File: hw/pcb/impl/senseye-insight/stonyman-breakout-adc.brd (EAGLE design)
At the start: 30.5 x 9.8 mm, 8 parts

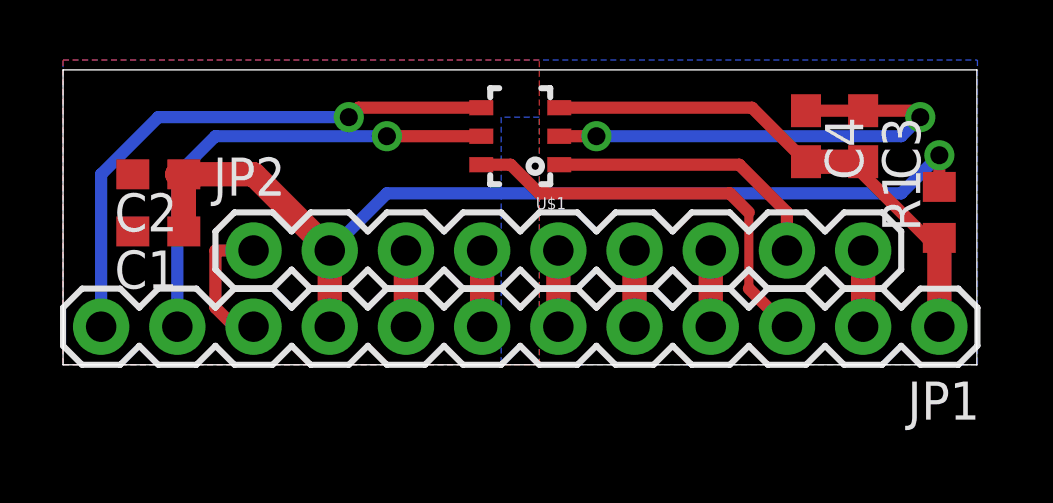
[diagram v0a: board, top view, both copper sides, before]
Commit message: better isolation of the SPI lines and GND
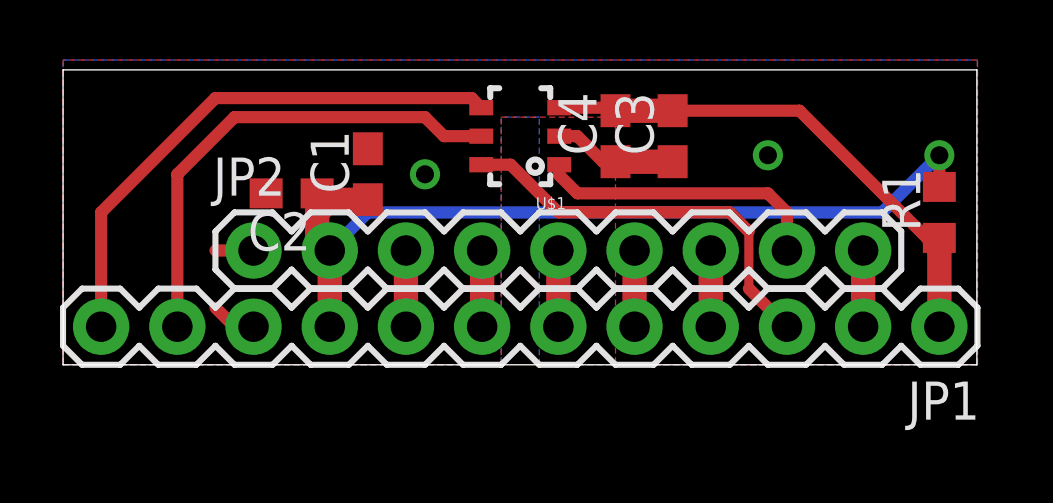
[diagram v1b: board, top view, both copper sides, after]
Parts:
- moved C1 7.24 mm to (10.2, 6.35), turned to 90 degrees
- moved C3 6.35 mm to (20.3, 7.62), turned to 90 degrees
- moved C4 6.35 mm to (18.4, 7.62), turned to 90 degrees
- moved C2 4.49 mm to (7.62, 5.71)
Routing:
- net GND: track 20.9 -> 6.97 mm
- net V_STONY: track 35.3 -> 29.2 mm
- net V_ADC: track 17.3 -> 18.0 mm
- net ADC-MISO: track 15.7 -> 16.3 mm, vias 1 -> 0
- net ADC-SCLK: track 18.7 -> 18.2 mm, vias 1 -> 0

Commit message: pretty sure this is finished but needs to pass DRC
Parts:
- moved C1 0.63 mm to (10.2, 5.71), turned to 0 degrees
- moved C2 0.63 mm to (6.99, 5.71)
- moved C3 0.63 mm to (20.3, 6.99)
- moved C4 0.63 mm to (18.4, 6.99)
- moved U$1 0.63 mm to (15.2, 6.99)
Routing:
- net V_STONY: track 29.2 -> 30.6 mm
- net ADC-MISO: track 16.3 -> 17.6 mm
- net ANALOG: track 9.72 -> 8.88 mm
- net GND: track 6.97 -> 6.94 mm, vias 2 -> 3

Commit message: added one more extra piece of GND routing
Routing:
- net GND: track 6.94 -> 9.48 mm
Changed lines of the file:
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@@
 <via x="12.7" y="5.715" extent="1-16" drill="0.6"/>
 <via x="3.81" y="4.445" extent="1-16" drill="0.6"/>
+<wire x1="6.35" y1="3.81" x2="6.35" y2="6.35" width="0.4064" layer="1"/>
 </signal>
 <signal name="V_STONY">

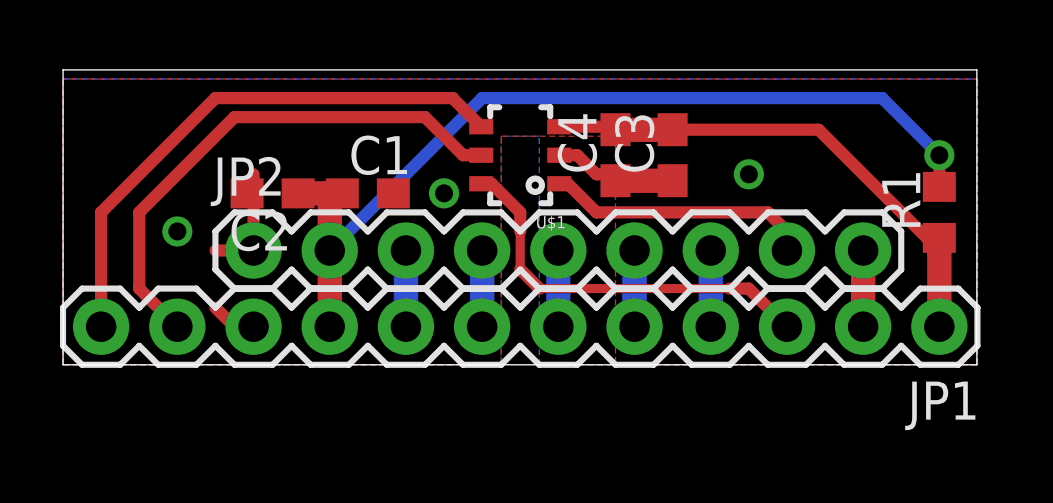
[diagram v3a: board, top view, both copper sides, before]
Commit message: made the board even tighter
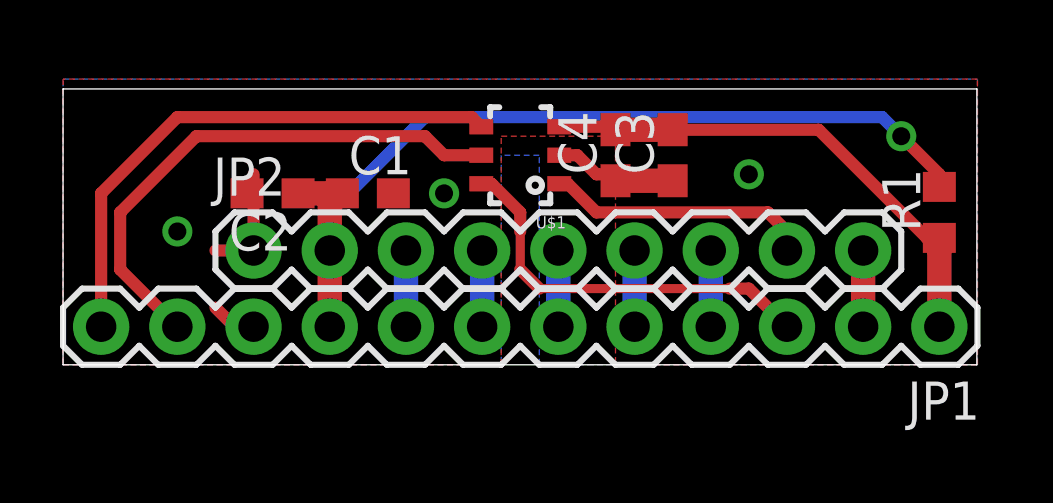
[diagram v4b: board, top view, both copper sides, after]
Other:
- board size 30.5 x 9.8 mm -> 30.5 x 9.2 mm
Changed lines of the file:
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@@
 <plain>
 <wire x1="0" y1="0" x2="30.46" y2="0" width="0" layer="20"/>
-<wire x1="30.46" y1="0" x2="30.46" y2="9.83" width="0" layer="20"/>
-<wire x1="30.46" y1="9.83" x2="0" y2="9.83" width="0" layer="20"/>
-<wire x1="0" y1="9.83" x2="0" y2="0" width="0" layer="20"/>
+<wire x1="30.46" y1="0" x2="30.46" y2="9.195" width="0" layer="20"/>
+<wire x1="30.46" y1="9.195" x2="0" y2="9.195" width="0" layer="20"/>
+<wire x1="0" y1="9.195" x2="0" y2="0" width="0" layer="20"/>
 </plain>
 <attributes>
@@
 </class>
 </classes>
-<designrules name="default">
-<description language="de">&lt;b&gt;EAGLE Design Rules&lt;/b&gt;
+<designrules name="sunstone-2lyr_v1.0.0.3">
+<description language="en">&lt;b&gt;EAGLE Design Rules for *2* Layer Designs (DS)&lt;/b&gt;
 &lt;p&gt;
-Die Standard-Design-Rules sind so gewählt, dass sie für
-die meisten Anwendungen passen. Sollte ihre Platine
-besondere Anforderungen haben, treffen Sie die erforderlichen
-Einstellungen hier und speichern die Design Rules unter
-einem neuen Namen ab.</description>
-<description language="en">&lt;b&gt;EAGLE Design Rules&lt;/b&gt;
+This Sunstone Circuits 2 Layer .DRU has been set to cover our minimum requirements for our double sided products. For questions, comments, suggestions, please contact Sunstone Customer Support: &lt;p&gt;&lt;b&gt;Email:&lt;/b&gt;  mailto:support@sunstone.com&lt;br&gt;&lt;b&gt;Phone:&lt;/b&gt; 800-228-8198.&lt;p&gt; v1.1Mod10/16/07~Layers-core reversal.Distance C/D.Restring%.Supply G%.&lt;p&gt; v1.2 Mod12/06/07~Distance C/D to 20mils.&lt;p&gt;v1.3Mod12/12/07~Supply/Annulus Value to 12.5mils&lt;p&gt;1/15/08 SSC-EAGLE-2Lyr_v1.0.0.3~For Release&lt;p&gt;10/3/08 Description Edit.&lt;p&gt;
 &lt;p&gt;
-The default Design Rules have been set to cover
-a wide range of applications. Your particular design
-may have different requirements, so please make the
-necessary adjustments and save your customized
-design rules under a new name.</description>
+&lt;i&gt;Attention: Upon running the design check and making modifications, please remember to save any changes before closing the application and sending in your board file to Sunstone Circuits for conversion.&lt;i&gt;</description>
 <param name="layerSetup" value="(1*16)"/>
-<param name="mtCopper" value="0.035mm 0.035mm 0.035mm 0.035mm 0.035mm 0.035mm 0.035mm 0.035mm 0.035mm 0.035mm 0.035mm 0.035mm 0.035mm 0.035mm 0.035mm 0.035mm"/>
-<param name="mtIsolate" value="1.5mm 0.15mm 0.2mm 0.15mm 0.2mm 0.15mm 0.2mm 0.15mm 0.2mm 0.15mm 0.2mm 0.15mm 0.2mm 0.15mm 0.2mm"/>
-<param name="mdWireWire" value="8mil"/>
-<param name="mdWirePad" value="8mil"/>
-<param name="mdWireVia" value="8mil"/>
-<param name="mdPadPad" value="8mil"/>
-<param name="mdPadVia" value="8mil"/>
-<param name="mdViaVia" value="8mil"/>
-<param name="mdSmdPad" value="8mil"/>
-<param name="mdSmdVia" value="8mil"/>
-<param name="mdSmdSmd" value="8mil"/>
+<param name="mtCopper" value="0.0178mm 0.0356mm 0.0356mm 0.0356mm 0.0356mm 0.0356mm 0.0356mm 0.0356mm 0.0356mm 0.0356mm 0.0356mm 0.0356mm 0.0356mm 0.0356mm 0.0356mm 0.0178mm"/>
+<param name="mtIsolate" value="59mil 0.1499mm 0.2007mm 0.1499mm 0.2007mm 0.1499mm 0.2007mm 0.1499mm 0.2007mm 0.1499mm 0.2007mm 0.1499mm 0.2007mm 0.1499mm 0.2007mm"/>
+<param name="mdWireWire" value="6mil"/>
+<param name="mdWirePad" value="6mil"/>
+<param name="mdWireVia" value="6mil"/>
+<param name="mdPadPad" value="6mil"/>
+<param name="mdPadVia" value="6mil"/>
+<param name="mdViaVia" value="6mil"/>
+<param name="mdSmdPad" value="6mil"/>
+<param name="mdSmdVia" value="6mil"/>
+<param name="mdSmdSmd" value="6mil"/>
 <param name="mdViaViaSameLayer" value="8mil"/>
 <param name="mnLayersViaInSmd" value="2"/>
-<param name="mdCopperDimension" value="40mil"/>
-<param name="mdDrill" value="8mil"/>
+<param name="mdCopperDimension" value="20mil"/>
+<param name="mdDrill" value="16mil"/>
 <param name="mdSmdStop" value="0mil"/>
-<param name="msWidth" value="10mil"/>
-<param name="msDrill" value="24mil"/>
-<param name="msMicroVia" value="9.99mm"/>
+<param name="msWidth" value="6mil"/>
+<param name="msDrill" value="14mil"/>
+<param name="msMicroVia" value="9.9898mm"/>
 <param name="msBlindViaRatio" value="0.5"/>
 <param name="rvPadTop" value="0.25"/>
@@
 <param name="rvMicroViaOuter" value="0.25"/>
 <param name="rvMicroViaInner" value="0.25"/>
-<param name="rlMinPadTop" value="10mil"/>
-<param name="rlMaxPadTop" value="20mil"/>
-<param name="rlMinPadInner" value="10mil"/>
-<param name="rlMaxPadInner" value="20mil"/>
-<param name="rlMinPadBottom" value="10mil"/>
-<param name="rlMaxPadBottom" value="20mil"/>
+<param name="rlMinPadTop" value="8mil"/>
+<param name="rlMaxPadTop" value="999mil"/>
+<param name="rlMinPadInner" value="0mil"/>
+<param name="rlMaxPadInner" value="0mil"/>
+<param name="rlMinPadBottom" value="8mil"/>
+<param name="rlMaxPadBottom" value="999mil"/>
 <param name="rlMinViaOuter" value="8mil"/>
-<param name="rlMaxViaOuter" value="20mil"/>
-<param name="rlMinViaInner" value="8mil"/>
-<param name="rlMaxViaInner" value="20mil"/>
-<param name="rlMinMicroViaOuter" value="4mil"/>
-<param name="rlMaxMicroViaOuter" value="20mil"/>
-<param name="rlMinMicroViaInner" value="4mil"/>
-<param name="rlMaxMicroViaInner" value="20mil"/>
+<param name="rlMaxViaOuter" value="999mil"/>
+<param name="rlMinViaInner" value="0mil"/>
+<param name="rlMaxViaInner" value="0mil"/>
+<param name="rlMinMicroViaOuter" value="8mil"/>
+<param name="rlMaxMicroViaOuter" value="999mil"/>
+<param name="rlMinMicroViaInner" value="0mil"/>
+<param name="rlMaxMicroViaInner" value="0mil"/>
 <param name="psTop" value="-1"/>
 <param name="psBottom" value="-1"/>
@@
 <param name="mvStopFrame" value="1"/>
 <param name="mvCreamFrame" value="0"/>
-<param name="mlMinStopFrame" value="4mil"/>
-<param name="mlMaxStopFrame" value="4mil"/>
+<param name="mlMinStopFrame" value="3mil"/>
+<param name="mlMaxStopFrame" value="3mil"/>
 <param name="mlMinCreamFrame" value="0mil"/>
 <param name="mlMaxCreamFrame" value="0mil"/>
@@
 <param name="checkRestrict" value="1"/>
 <param name="useDiameter" value="13"/>
-<param name="maxErrors" value="50"/>
+<param name="maxErrors" value="500"/>
 </designrules>
 <autorouter>
@@
 <vertex x="30.48" y="0"/>
 <vertex x="15.875" y="0"/>
-<vertex x="15.875" y="7.62"/>
-<vertex x="14.605" y="7.62"/>
+<vertex x="15.875" y="6.985"/>
+<vertex x="14.605" y="6.985"/>
 <vertex x="14.605" y="0"/>
 <vertex x="0" y="0"/>
@@
 <contactref element="JP2" pad="2"/>
 <wire x1="8.89" y1="1.27" x2="8.89" y2="3.81" width="0.8128" layer="1"/>
-<via x="29.21" y="6.985" extent="1-16" drill="0.6"/>
-<wire x1="29.21" y1="6.985" x2="29.21" y2="5.93" width="0.4064" layer="1"/>
-<wire x1="8.89" y1="3.81" x2="13.97" y2="8.89" width="0.4064" layer="16"/>
-<wire x1="13.97" y1="8.89" x2="27.305" y2="8.89" width="0.4064" layer="16"/>
-<wire x1="27.305" y1="8.89" x2="29.21" y2="6.985" width="0.4064" layer="16"/>
 <wire x1="7.835" y1="5.715" x2="9.31" y2="5.715" width="0.8128" layer="1"/>
 <wire x1="9.31" y1="5.715" x2="8.89" y2="5.715" width="0.8128" layer="1"/>
 <wire x1="8.89" y1="5.715" x2="8.89" y2="3.81" width="0.8128" layer="1"/>
+<wire x1="29.21" y1="5.93" x2="29.21" y2="6.35" width="0.4064" layer="1"/>
+<wire x1="29.21" y1="6.35" x2="27.94" y2="7.62" width="0.4064" layer="1"/>
+<via x="27.94" y="7.62" extent="1-16" drill="0.6"/>
+<wire x1="27.94" y1="7.62" x2="27.305" y2="8.255" width="0.4064" layer="16"/>
+<wire x1="27.305" y1="8.255" x2="12.065" y2="8.255" width="0.4064" layer="16"/>
+<wire x1="12.065" y1="8.255" x2="8.89" y2="5.08" width="0.4064" layer="16"/>
+<wire x1="8.89" y1="5.08" x2="8.89" y2="3.81" width="0.4064" layer="16"/>
 </signal>
 <signal name="RESP">
@@
 <contactref element="U$1" pad="5"/>
 <contactref element="JP1" pad="11"/>
-<wire x1="13.94" y1="6.985" x2="13.335" y2="6.985" width="0.4064" layer="1"/>
-<wire x1="13.335" y1="6.985" x2="12.065" y2="8.255" width="0.4064" layer="1"/>
-<wire x1="12.065" y1="8.255" x2="5.715" y2="8.255" width="0.4064" layer="1"/>
-<wire x1="5.715" y1="8.255" x2="2.54" y2="5.08" width="0.4064" layer="1"/>
-<wire x1="2.54" y1="5.08" x2="2.54" y2="2.54" width="0.4064" layer="1"/>
-<wire x1="2.54" y1="2.54" x2="3.81" y2="1.27" width="0.4064" layer="1"/>
+<wire x1="13.94" y1="6.985" x2="12.7" y2="6.985" width="0.4064" layer="1"/>
+<wire x1="12.7" y1="6.985" x2="12.065" y2="7.62" width="0.4064" layer="1"/>
+<wire x1="12.065" y1="7.62" x2="4.445" y2="7.62" width="0.4064" layer="1"/>
+<wire x1="4.445" y1="7.62" x2="1.905" y2="5.08" width="0.4064" layer="1"/>
+<wire x1="1.905" y1="5.08" x2="1.905" y2="3.175" width="0.4064" layer="1"/>
+<wire x1="1.905" y1="3.175" x2="3.81" y2="1.27" width="0.4064" layer="1"/>
 </signal>
 <signal name="ADC-SCLK">
 <contactref element="U$1" pad="4"/>
 <contactref element="JP1" pad="12"/>
-<wire x1="13.94" y1="7.935" x2="12.985" y2="8.89" width="0.4064" layer="1"/>
-<wire x1="12.985" y1="8.89" x2="5.08" y2="8.89" width="0.4064" layer="1"/>
-<wire x1="5.08" y1="8.89" x2="1.27" y2="5.08" width="0.4064" layer="1"/>
-<wire x1="1.27" y1="5.08" x2="1.27" y2="1.27" width="0.4064" layer="1"/>
+<wire x1="13.94" y1="7.935" x2="13.62" y2="8.255" width="0.4064" layer="1"/>
+<wire x1="13.62" y1="8.255" x2="3.81" y2="8.255" width="0.4064" layer="1"/>
+<wire x1="3.81" y1="8.255" x2="1.27" y2="5.715" width="0.4064" layer="1"/>
+<wire x1="1.27" y1="5.715" x2="1.27" y2="1.27" width="0.4064" layer="1"/>
 </signal>
 <signal name="ADC-SS">

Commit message: fixed almost all the DRC errors
most were related to components and traces being too close to the board
edge. there are still some keepout errors (with 0603 caps which I won't
fix), and the analog line is justg a little too close to the headers
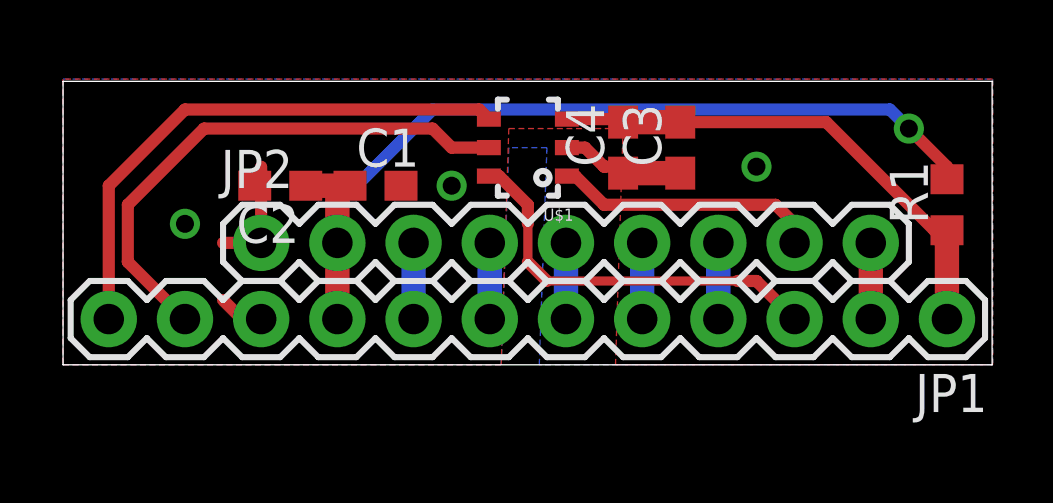
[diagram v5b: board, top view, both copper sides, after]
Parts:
- moved C3 0.36 mm to (20.6, 7.24)
- moved C4 0.36 mm to (18.7, 7.24)
- moved JP2 0.36 mm to (6.60, 4.06)
- moved C1 0.36 mm to (10.4, 5.97)
- moved C2 0.36 mm to (7.24, 5.97)
- moved U$1 0.36 mm to (15.5, 7.24)
- moved JP1 0.36 mm to (29.5, 1.52)
- moved R1 0.36 mm to (29.5, 5.33)
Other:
- board size 30.5 x 9.2 mm -> 31 x 9.4 mm

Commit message: fixed all DRC errors (including the 0603 caps)
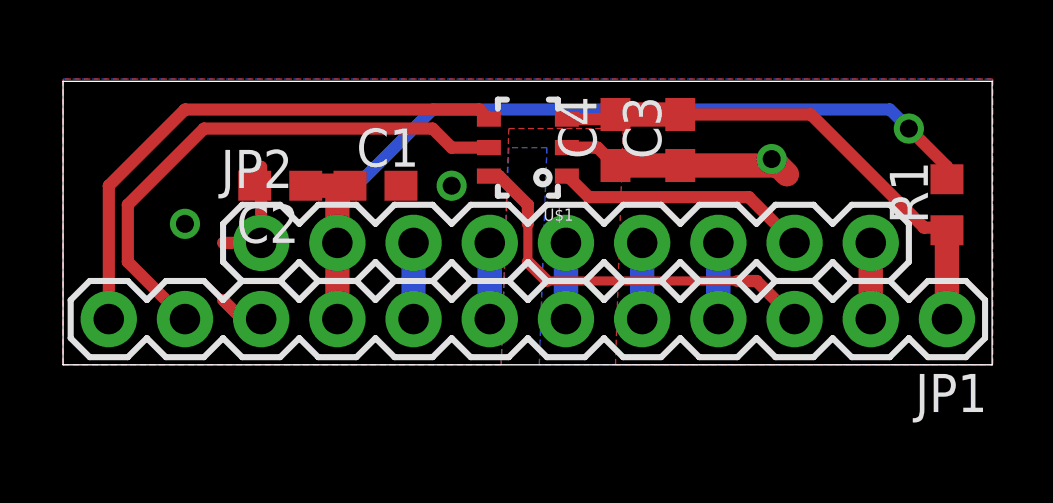
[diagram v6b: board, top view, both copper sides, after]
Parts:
- moved C4 0.36 mm to (18.4, 7.49)
- moved C3 0.25 mm to (20.6, 7.49)
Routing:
- net GND: track 9.48 -> 13.0 mm
